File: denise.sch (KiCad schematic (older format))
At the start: 51 parts, among them CN202 DB23_Female, CN203 Conn_02x18_Odd_Even, CN206 COMPOSITE, CN207 INTERNAL VIDEO SLOT, U201 DENISE8373, U205 74LS244, U206 74LS244, U303 74F08

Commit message: REV 6.2 fixes applied
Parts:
- removed EMI200: C_Feedthrough, symbol Device:C_Feedthrough
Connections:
- net +5V_USER: now also R215.2
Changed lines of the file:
@@
 _BHS
-$Comp
-L power:+5V #PWR0218
-U 1 1 6FF373F7
-P 6800 4350
-F 0 "#PWR0218" H 6800 4200 50  0001 C CNN
-F 1 "+5V" V 6815 4478 50  0000 L CNN
-F 2 "" H 6800 4350 50  0001 C CNN
-F 3 "" H 6800 4350 50  0001 C CNN
-	1    6800 4350
-	0    1    1    0
-$EndComp
 $Comp
 L power:GND #PWR0213
@@
 $EndComp
 $Comp
-L Device:C_Feedthrough EMI200
-U 1 1 6FF38969
-P 6600 4250
-F 0 "EMI200" H 6700 4250 50  0000 C CNN
-F 1 "C_Feedthrough" H 6600 4464 50  0001 C CNN
-F 2 "" V 6600 4250 50  0001 C CNN
-F 3 "~" V 6600 4250 50  0001 C CNN
-	1    6600 4250
-	-1   0    0    1
-$EndComp
-$Comp
-L power:GND #PWR0217
-U 1 1 6FF392C9
-P 6600 4150
-F 0 "#PWR0217" H 6600 3900 50  0001 C CNN
-F 1 "GND" H 6605 3977 50  0000 C CNN
-F 2 "" H 6600 4150 50  0001 C CNN
-F 3 "" H 6600 4150 50  0001 C CNN
-	1    6600 4150
-	1    0    0    1
-$EndComp
-$Comp
 L Device:R R215
 U 1 1 6FF3A009
@@
 $EndComp
 Connection ~ 2100 6100
+Text GLabel 6400 4350 2    50   Input ~ 0
++5V_USER
 $EndSCHEMATC

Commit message: Add gender to connectors
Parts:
- CN202: Gender (none) -> Male
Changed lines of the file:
@@
 F 2 "" H 12450 4750 50  0001 C CNN
 F 3 " ~" H 12450 4750 50  0001 C CNN
+F 4 "Male" H 12500 4850 50  0001 C CNN "Gender"
 	1    12500 4850
 	-1   0    0    -1

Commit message: All reviews done
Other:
- moved on the sheet: C201, C205, C206, C214, C215, C216, C217, C226, C913, C914, C915, CN202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

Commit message: Associate footprints with components
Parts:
- CN203: footprint (none) -> Connector_PinSocket_2.54mm:PinSocket_2x18_P2.54mm_Vertical
- EMI201, EMI206, EMI207, EMI208, EMI209, EMI210, EMI211, EMI229: footprint (none) -> Connector_PinSocket_2.54mm:PinSocket_1x03_P2.54mm_Vertical
- F5: footprint (none) -> Fuse:Fuse_Littelfuse-LVR100
- FB216, FB217, FB218, FB219, FB220, FB221, FB900, FB901, FB902, FB903: footprint (none) -> Inductor_THT:L_Axial_L7.0mm_D3.3mm_P5.08mm_Vertical_Fastron_MICC
- HY200: footprint (none) -> Connector_PinSocket_2.54mm:PinSocket_1x22_P2.54mm_Vertical
- R203, R211, R212, R215, R216: footprint (none) -> Resistor_THT:R_Axial_DIN0207_L6.3mm_D2.5mm_P10.16mm_Horizontal
- U201: footprint (none) -> Package_DIP:DIP-48_W15.24mm_Socket
- U205, U206: footprint (none) -> Package_DIP:DIP-20_W7.62mm_Socket
- U303: footprint (none) -> Package_DIP:DIP-14_W7.62mm_Socket
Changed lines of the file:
@@
 F 0 "U201" H 3450 3925 50  0000 C CNN
 F 1 "DENISE8373" H 3450 3834 50  0000 C CNN
-F 2 "" H 3450 3800 50  0001 C CNN
+F 2 "Package_DIP:DIP-48_W15.24mm_Socket" H 3450 3800 50  0001 C CNN
 F 3 "" H 3450 3800 50  0001 C CNN
 	1    3450 3750
@@
 F 0 "HY200" H 9200 5575 50  0000 C CNN
 F 1 "HY200VIDIOT" H 9200 5484 50  0000 C CNN
-F 2 "" H 9200 5450 50  0001 C CNN
+F 2 "Connector_PinSocket_2.54mm:PinSocket_1x22_P2.54mm_Vertical" H 9200 5450 50  0001 C CNN
 F 3 "" H 9200 5450 50  0001 C CNN
 	1    9200 5400
@@
 F 0 "CN203" V 9250 4179 50  0000 L CNN
 F 1 "Conn_02x18_Odd_Even" V 9205 4179 50  0001 L CNN
-F 2 "" H 9200 3300 50  0001 C CNN
+F 2 "Connector_PinSocket_2.54mm:PinSocket_2x18_P2.54mm_Vertical" H 9200 3300 50  0001 C CNN
 F 3 "~" H 9200 3300 50  0001 C CNN
 	1    9200 3300
@@
 F 0 "U205" H 6400 3619 50  0000 C CNN
 F 1 "74LS244" H 6400 3710 50  0000 C CNN
-F 2 "" H 6400 4600 50  0001 C CNN
+F 2 "Package_DIP:DIP-20_W7.62mm_Socket" H 6400 4600 50  0001 C CNN
 F 3 "http://www.ti.com/lit/gpn/sn74LS244" H 6400 4600 50  0001 C CNN
 	1    6400 4600
@@
 F 0 "U206" H 6400 7581 50  0000 C CNN
 F 1 "74LS244" H 6400 7490 50  0000 C CNN
-F 2 "" H 6400 6600 50  0001 C CNN
+F 2 "Package_DIP:DIP-20_W7.62mm_Socket" H 6400 6600 50  0001 C CNN
 F 3 "http://www.ti.com/lit/gpn/sn74LS244" H 6400 6600 50  0001 C CNN
 	1    6400 6600
@@
 F 0 "EMI201" H 11300 3463 50  0000 C CNN
 F 1 "C_Feedthrough" H 11300 3464 50  0001 C CNN
-F 2 "" V 11300 3250 50  0001 C CNN
+F 2 "Connector_PinSocket_2.54mm:PinSocket_1x03_P2.54mm_Vertical" V 11300 3250 50  0001 C CNN
 F 3 "~" V 11300 3250 50  0001 C CNN
 	1    11300 3250
@@
 F 0 "EMI208" H 13750 3963 50  0000 C CNN
 F 1 "C_Feedthrough" H 13750 3964 50  0001 C CNN
-F 2 "" V 13750 3750 50  0001 C CNN
+F 2 "Connector_PinSocket_2.54mm:PinSocket_1x03_P2.54mm_Vertical" V 13750 3750 50  0001 C CNN
 F 3 "~" V 13750 3750 50  0001 C CNN
 	1    13750 3750
@@
 F 0 "EMI206" H 12300 7350 50  0000 C CNN
 F 1 "C_Feedthrough" H 12200 7564 50  0001 C CNN
-F 2 "" V 12200 7350 50  0001 C CNN
+F 2 "Connector_PinSocket_2.54mm:PinSocket_1x03_P2.54mm_Vertical" V 12200 7350 50  0001 C CNN
 F 3 "~" V 12200 7350 50  0001 C CNN
 	1    12200 7350
@@
 F 0 "EMI207" H 12400 7600 50  0000 C CNN
 F 1 "C_Feedthrough" H 12300 7814 50  0001 C CNN
-F 2 "" V 12300 7600 50  0001 C CNN
+F 2 "Connector_PinSocket_2.54mm:PinSocket_1x03_P2.54mm_Vertical" V 12300 7600 50  0001 C CNN
 F 3 "~" V 12300 7600 50  0001 C CNN
 	1    12300 7600
@@
 F 0 "EMI209" H 13800 8813 50  0000 C CNN
 F 1 "C_Feedthrough" H 13800 8814 50  0001 C CNN
-F 2 "" V 13800 8600 50  0001 C CNN
+F 2 "Connector_PinSocket_2.54mm:PinSocket_1x03_P2.54mm_Vertical" V 13800 8600 50  0001 C CNN
 F 3 "~" V 13800 8600 50  0001 C CNN
 	1    13800 8600
@@
 F 0 "EMI229" H 2400 8263 50  0000 C CNN
 F 1 "C_Feedthrough" H 2400 8264 50  0001 C CNN
-F 2 "" V 2400 8050 50  0001 C CNN
+F 2 "Connector_PinSocket_2.54mm:PinSocket_1x03_P2.54mm_Vertical" V 2400 8050 50  0001 C CNN
 F 3 "~" V 2400 8050 50  0001 C CNN
 	1    2400 8050
@@
 F 0 "F5" V 14045 7900 50  0000 C CNN
 F 1 "Fuse" V 14044 7900 50  0001 C CNN
-F 2 "" V 14080 7900 50  0001 C CNN
+F 2 "Fuse:Fuse_Littelfuse-LVR100" V 14080 7900 50  0001 C CNN
 F 3 "~" H 14150 7900 50  0001 C CNN
 	1    14150 7900
@@
 F 0 "FB216" V 12150 5350 50  0000 C CNN
 F 1 "Ferrite_Bead_Small" V 12104 5250 50  0001 C CNN
-F 2 "" V 12180 5250 50  0001 C CNN
+F 2 "Inductor_THT:L_Axial_L7.0mm_D3.3mm_P5.08mm_Vertical_Fastron_MICC" V 12180 5250 50  0001 C CNN
 F 3 "~" H 12250 5250 50  0001 C CNN
 	1    12250 5250
@@
 F 0 "FB217" V 12150 5550 50  0000 C CNN
 F 1 "Ferrite_Bead_Small" V 12104 5450 50  0001 C CNN
-F 2 "" V 12180 5450 50  0001 C CNN
+F 2 "Inductor_THT:L_Axial_L7.0mm_D3.3mm_P5.08mm_Vertical_Fastron_MICC" V 12180 5450 50  0001 C CNN
 F 3 "~" H 12250 5450 50  0001 C CNN
 	1    12250 5450
@@
 F 0 "FB900" V 12150 5750 50  0000 C CNN
 F 1 "Ferrite_Bead_Small" V 12104 5650 50  0001 C CNN
-F 2 "" V 12180 5650 50  0001 C CNN
+F 2 "Inductor_THT:L_Axial_L7.0mm_D3.3mm_P5.08mm_Vertical_Fastron_MICC" V 12180 5650 50  0001 C CNN
 F 3 "~" H 12250 5650 50  0001 C CNN
 	1    12250 5650
@@
 F 0 "FB901" V 12150 5950 50  0000 C CNN
 F 1 "Ferrite_Bead_Small" V 12104 5850 50  0001 C CNN
-F 2 "" V 12180 5850 50  0001 C CNN
+F 2 "Inductor_THT:L_Axial_L7.0mm_D3.3mm_P5.08mm_Vertical_Fastron_MICC" V 12180 5850 50  0001 C CNN
 F 3 "~" H 12250 5850 50  0001 C CNN
 	1    12250 5850
@@
 F 0 "FB902" V 12150 6150 50  0000 C CNN
 F 1 "Ferrite_Bead_Small" V 12104 6050 50  0001 C CNN
-F 2 "" V 12180 6050 50  0001 C CNN
+F 2 "Inductor_THT:L_Axial_L7.0mm_D3.3mm_P5.08mm_Vertical_Fastron_MICC" V 12180 6050 50  0001 C CNN
 F 3 "~" H 12250 6050 50  0001 C CNN
 	1    12250 6050
@@
 F 0 "FB218" V 12150 6350 50  0000 C CNN
 F 1 "Ferrite_Bead_Small" V 12104 6250 50  0001 C CNN
-F 2 "" V 12180 6250 50  0001 C CNN
+F 2 "Inductor_THT:L_Axial_L7.0mm_D3.3mm_P5.08mm_Vertical_Fastron_MICC" V 12180 6250 50  0001 C CNN
 F 3 "~" H 12250 6250 50  0001 C CNN
 	1    12250 6250
@@
 F 0 "FB219" V 12150 6550 50  0000 C CNN
 F 1 "Ferrite_Bead_Small" V 12104 6450 50  0001 C CNN
-F 2 "" V 12180 6450 50  0001 C CNN
+F 2 "Inductor_THT:L_Axial_L7.0mm_D3.3mm_P5.08mm_Vertical_Fastron_MICC" V 12180 6450 50  0001 C CNN
 F 3 "~" H 12250 6450 50  0001 C CNN
 	1    12250 6450
@@
 F 0 "FB220" V 12150 6750 50  0000 C CNN
 F 1 "Ferrite_Bead_Small" V 12104 6650 50  0001 C CNN
-F 2 "" V 12180 6650 50  0001 C CNN
+F 2 "Inductor_THT:L_Axial_L7.0mm_D3.3mm_P5.08mm_Vertical_Fastron_MICC" V 12180 6650 50  0001 C CNN
 F 3 "~" H 12250 6650 50  0001 C CNN
 	1    12250 6650
@@
 F 0 "FB221" V 12150 6950 50  0000 C CNN
 F 1 "Ferrite_Bead_Small" V 12104 6850 50  0001 C CNN
-F 2 "" V 12180 6850 50  0001 C CNN
+F 2 "Inductor_THT:L_Axial_L7.0mm_D3.3mm_P5.08mm_Vertical_Fastron_MICC" V 12180 6850 50  0001 C CNN
 F 3 "~" H 12250 6850 50  0001 C CNN
 	1    12250 6850
@@
 F 0 "FB903" V 12150 7150 50  0000 C CNN
 F 1 "Ferrite_Bead_Small" V 12104 7050 50  0001 C CNN
-F 2 "" V 12180 7050 50  0001 C CNN
+F 2 "Inductor_THT:L_Axial_L7.0mm_D3.3mm_P5.08mm_Vertical_Fastron_MICC" V 12180 7050 50  0001 C CNN
 F 3 "~" H 12250 7050 50  0001 C CNN
 	1    12250 7050
@@
 F 0 "EMI210" H 13800 8213 50  0000 C CNN
 F 1 "C_Feedthrough" H 13800 8214 50  0001 C CNN
-F 2 "" V 13800 8000 50  0001 C CNN
+F 2 "Connector_PinSocket_2.54mm:PinSocket_1x03_P2.54mm_Vertical" V 13800 8000 50  0001 C CNN
 F 3 "~" V 13800 8000 50  0001 C CNN
 	1    13800 8000
@@
 F 0 "EMI211" H 14150 7363 50  0000 C CNN
 F 1 "C_Feedthrough" H 14150 7364 50  0001 C CNN
-F 2 "" V 14150 7150 50  0001 C CNN
+F 2 "Connector_PinSocket_2.54mm:PinSocket_1x03_P2.54mm_Vertical" V 14150 7150 50  0001 C CNN
 F 3 "~" V 14150 7150 50  0001 C CNN
 	1    14150 7150
@@
 F 0 "R211" H 12170 2546 50  0000 L CNN
 F 1 "10k" H 12170 2455 50  0000 L CNN
-F 2 "" V 12030 2500 50  0001 C CNN
+F 2 "Resistor_THT:R_Axial_DIN0207_L6.3mm_D2.5mm_P10.16mm_Horizontal" V 12030 2500 50  0001 C CNN
 F 3 "~" H 12100 2500 50  0001 C CNN
 	1    12100 2500
@@
 F 0 "R216" H 12570 2546 50  0000 L CNN
 F 1 "10k" H 12570 2455 50  0000 L CNN
-F 2 "" V 12430 2500 50  0001 C CNN
+F 2 "Resistor_THT:R_Axial_DIN0207_L6.3mm_D2.5mm_P10.16mm_Horizontal" V 12430 2500 50  0001 C CNN
 F 3 "~" H 12500 2500 50  0001 C CNN
 	1    12500 2500
@@
 F 0 "U303" H 12950 3175 50  0000 C CNN
 F 1 "74F08" H 12950 3084 50  0000 C CNN
-F 2 "" H 12950 2850 50  0001 C CNN
+F 2 "Package_DIP:DIP-14_W7.62mm_Socket" H 12950 2850 50  0001 C CNN
 F 3 "http://www.ti.com/lit/gpn/sn74LS08" H 12950 2850 50  0001 C CNN
 	1    12950 2850
@@
 F 0 "R212" V 13193 2850 50  0000 C CNN
 F 1 "22" V 13284 2850 50  0000 C CNN
-F 2 "" V 13330 2850 50  0001 C CNN
+F 2 "Resistor_THT:R_Axial_DIN0207_L6.3mm_D2.5mm_P10.16mm_Horizontal" V 13330 2850 50  0001 C CNN
 F 3 "~" H 13400 2850 50  0001 C CNN
 	1    13400 2850
@@
 F 0 "R203" H 8620 8396 50  0000 L CNN
 F 1 "10k" H 8620 8305 50  0000 L CNN
-F 2 "" V 8480 8350 50  0001 C CNN
+F 2 "Resistor_THT:R_Axial_DIN0207_L6.3mm_D2.5mm_P10.16mm_Horizontal" V 8480 8350 50  0001 C CNN
 F 3 "~" H 8550 8350 50  0001 C CNN
 	1    8550 8350
@@
 F 0 "R215" H 6970 5696 50  0000 L CNN
 F 1 "1" H 6970 5605 50  0000 L CNN
-F 2 "" V 6830 5650 50  0001 C CNN
+F 2 "Resistor_THT:R_Axial_DIN0207_L6.3mm_D2.5mm_P10.16mm_Horizontal" V 6830 5650 50  0001 C CNN
 F 3 "~" H 6900 5650 50  0001 C CNN
 	1    6900 5650

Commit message: Associate more components
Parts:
- C214, C226: footprint (none) -> Capacitor_THT:CP_Radial_D10.0mm_P5.00mm
- CN203: value Conn_02x18_Odd_Even -> INTERNAL VIDEO SLOT TOP
- CN207: value INTERNAL VIDEO SLOT -> INTERNAL VIDEO SLOT BOT
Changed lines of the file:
@@
 P 5400 2950
 F 0 "CN207" V 5496 3830 50  0000 L CNN
-F 1 "INTERNAL VIDEO SLOT" V 5450 750 50  0000 L CNN
+F 1 "INTERNAL VIDEO SLOT BOT" V 5450 750 50  0000 L CNN
 F 2 "" H 5400 2950 50  0001 C CNN
 F 3 "~" H 5400 2950 50  0001 C CNN
@@
 P 9200 3300
 F 0 "CN203" V 9250 4179 50  0000 L CNN
-F 1 "Conn_02x18_Odd_Even" V 9205 4179 50  0001 L CNN
+F 1 "INTERNAL VIDEO SLOT TOP" V 9205 4179 50  0001 L CNN
 F 2 "Connector_PinSocket_2.54mm:PinSocket_2x18_P2.54mm_Vertical" H 9200 3300 50  0001 C CNN
 F 3 "~" H 9200 3300 50  0001 C CNN
@@
 F 0 "C226" H 10568 7396 50  0000 L CNN
 F 1 "470uF 16v" H 10568 7305 50  0000 L CNN
-F 2 "" H 10488 7200 50  0001 C CNN
+F 2 "Capacitor_THT:CP_Radial_D10.0mm_P5.00mm" H 10488 7200 50  0001 C CNN
 F 3 "~" H 10450 7350 50  0001 C CNN
 	1    10450 7350
@@
 F 0 "C214" H 11218 7396 50  0000 L CNN
 F 1 "470uF 16v" H 11218 7305 50  0000 L CNN
-F 2 "" H 11138 7200 50  0001 C CNN
+F 2 "Capacitor_THT:CP_Radial_D10.0mm_P5.00mm" H 11138 7200 50  0001 C CNN
 F 3 "~" H 11100 7350 50  0001 C CNN
 	1    11100 7350

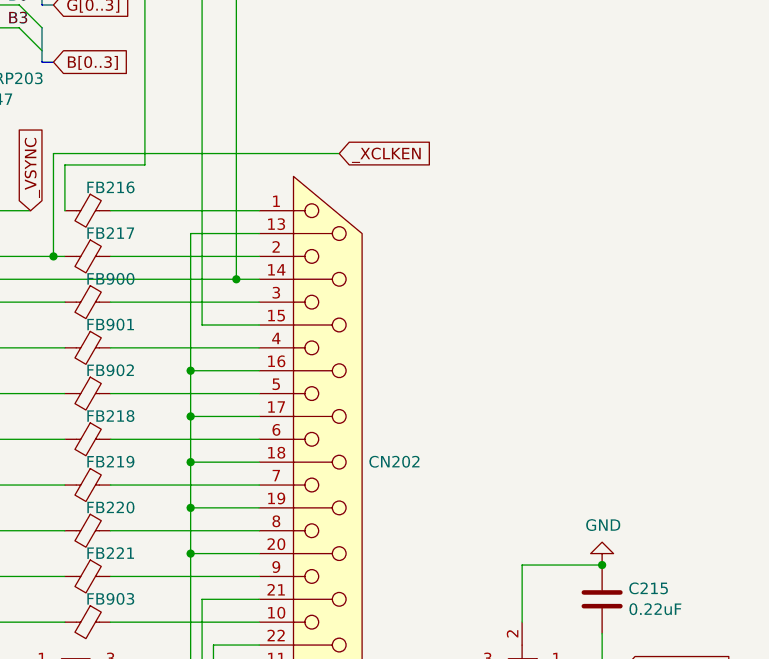
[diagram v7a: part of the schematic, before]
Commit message: Change namings
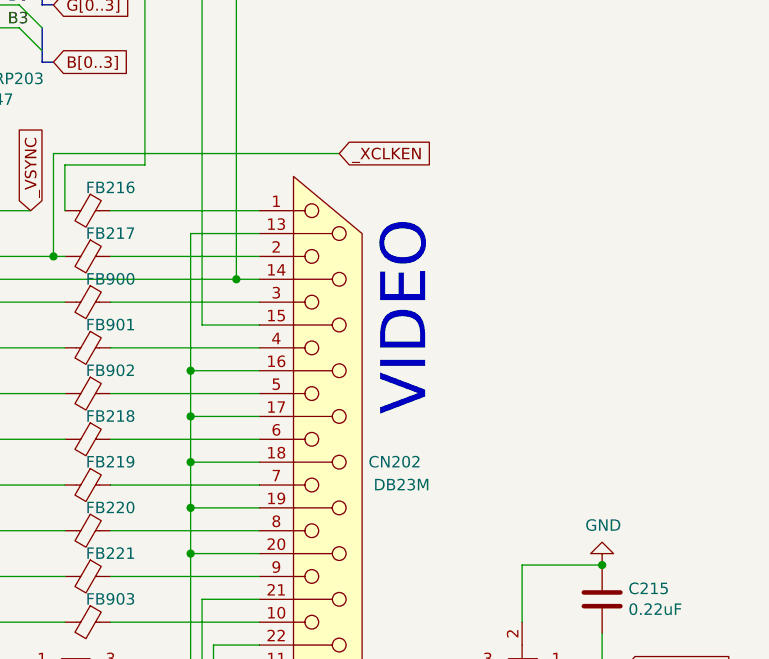
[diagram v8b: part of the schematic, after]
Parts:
- CN202: value DB23_Female -> DB23M
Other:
- note added: "VIDEO"
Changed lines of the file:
@@
 P 13250 6350
 F 0 "CN202" H 13022 6350 50  0000 R CNN
-F 1 "DB23_Female" H 13022 6305 50  0001 R CNN
+F 1 "DB23M" H 13000 6250 50  0000 R CNN
 F 2 "" H 13200 6250 50  0001 C CNN
 F 3 " ~" H 13200 6250 50  0001 C CNN
@@
 Wire Bus Line
 	2450 4050 2450 5650
+Text Notes 13750 6150 1    197  ~ 0
+VIDEO
 $EndSCHEMATC
